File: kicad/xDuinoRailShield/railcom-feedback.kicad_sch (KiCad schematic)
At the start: 8 parts, among them Q2 S8050, Q3 S8550, Q4 S8050, Q5 S8550

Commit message: Shield extracted
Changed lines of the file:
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@@
     (stroke (width 0) (type default))
   )
-  (label "RailCom feedback channel" (at 100.33 44.45 0) (fields_autoplaced)
+  (label "RailCom feedback generator" (at 100.33 44.45 0) (fields_autoplaced)
     (effects (font (size 3 3)) (justify left bottom))
   )

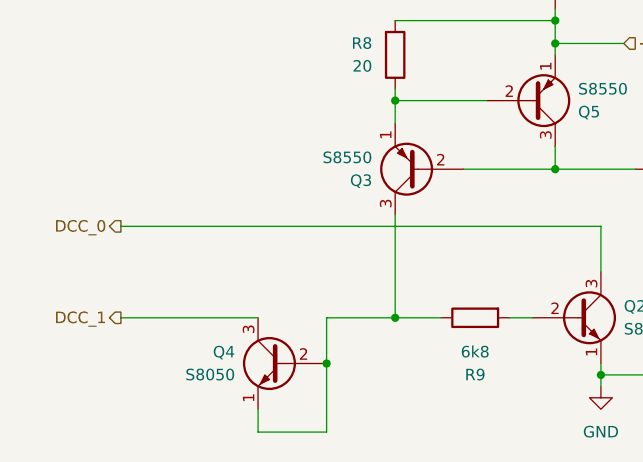
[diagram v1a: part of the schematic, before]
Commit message: More options, more Partnumbers
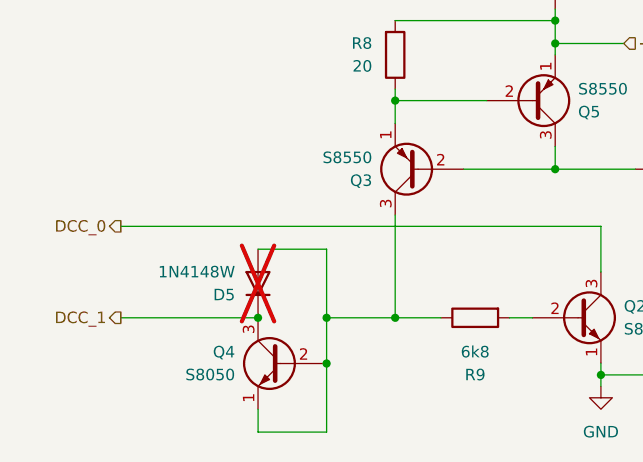
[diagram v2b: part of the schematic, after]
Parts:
- added D5: 1N4148W, Diode_SMD:D_SOD-123, symbol Diode:1N4148W
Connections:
- net DCC_1: now also D5.1 (K)
- net at Q3.3 (C), Q4.1 (E), Q4.2 (B)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: now also D5.2 (A)
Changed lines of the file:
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@@
   (junction (at 134.62 93.98) (diameter 0) (color 0 0 0 0)
   )
+  (junction (at 134.62 88.9) (diameter 0) (color 0 0 0 0)
+  )
+  (junction (at 127 88.9) (diameter 0) (color 0 0 0 0)
+  )
   (junction (at 160.02 72.39) (diameter 0) (color 0 0 0 0)
   )
@@
     (stroke (width 0) (type default))
   )
+  (wire (pts (xy 127 81.28) (xy 134.62 81.28))
+    (stroke (width 0) (type default))
+  )
   (wire (pts (xy 134.62 88.9) (xy 134.62 93.98))
     (stroke (width 0) (type default))
@@
   )
   (wire (pts (xy 181.61 72.39) (xy 176.53 72.39))
+    (stroke (width 0) (type default))
+  )
+  (wire (pts (xy 134.62 81.28) (xy 134.62 88.9))
     (stroke (width 0) (type default))
   )
@@
         )
         (path "/e63e39d7-6ac0-4ffd-8aa3-1841a4541b55/8dbd326e-72bb-40d4-858a-dc9fedaab895"
-          (reference "Q3") (unit 1)
+          (reference "Q403") (unit 1)
         )
       )
@@
         )
         (path "/e63e39d7-6ac0-4ffd-8aa3-1841a4541b55/8dbd326e-72bb-40d4-858a-dc9fedaab895"
-          (reference "Q2") (unit 1)
+          (reference "Q402") (unit 1)
         )
       )
@@
         )
         (path "/e63e39d7-6ac0-4ffd-8aa3-1841a4541b55/8dbd326e-72bb-40d4-858a-dc9fedaab895"
-          (reference "Q1") (unit 1)
+          (reference "Q401") (unit 1)
         )
       )
@@
         )
         (path "/e63e39d7-6ac0-4ffd-8aa3-1841a4541b55/8dbd326e-72bb-40d4-858a-dc9fedaab895"
-          (reference "R9") (unit 1)
+          (reference "R403") (unit 1)
         )
       )
@@
         )
         (path "/e63e39d7-6ac0-4ffd-8aa3-1841a4541b55/8dbd326e-72bb-40d4-858a-dc9fedaab895"
-          (reference "Q4") (unit 1)
+          (reference "Q404") (unit 1)
         )
       )
@@
         )
         (path "/e63e39d7-6ac0-4ffd-8aa3-1841a4541b55/8dbd326e-72bb-40d4-858a-dc9fedaab895"
-          (reference "#PWR012") (unit 1)
+          (reference "#PWR0402") (unit 1)
         )
       )
@@
         )
         (path "/e63e39d7-6ac0-4ffd-8aa3-1841a4541b55/8dbd326e-72bb-40d4-858a-dc9fedaab895"
-          (reference "#PWR011") (unit 1)
+          (reference "#PWR0401") (unit 1)
         )
       )
@@
         )
         (path "/e63e39d7-6ac0-4ffd-8aa3-1841a4541b55/8dbd326e-72bb-40d4-858a-dc9fedaab895"
-          (reference "R7") (unit 1)
+          (reference "R401") (unit 1)
         )
       )
@@
         )
         (path "/e63e39d7-6ac0-4ffd-8aa3-1841a4541b55/8dbd326e-72bb-40d4-858a-dc9fedaab895"
-          (reference "R8") (unit 1)
+          (reference "R402") (unit 1)
         )
       )
@@
         )
         (path "/e63e39d7-6ac0-4ffd-8aa3-1841a4541b55/8dbd326e-72bb-40d4-858a-dc9fedaab895"
-          (reference "JP_RAILCOM1") (unit 1)
-        )
-      )
+          (reference "JP_RAILCOM401") (unit 1)
+        )
+      )
+    )
+  )
+  (symbol (lib_id "Diode:1N4148W") (at 127 85.09 90) (unit 1)
+    (in_bom no) (on_board yes) (dnp yes)
+    (property "Reference" "D5" (at 124.46 86.36 90)
+      (effects (font (size 1.27 1.27)) (justify left))
+    )
+    (property "Value" "1N4148W" (at 124.46 83.82 90)
+      (effects (font (size 1.27 1.27)) (justify left))
+    )
+    (property "Footprint" "Diode_SMD:D_SOD-123" (at 131.445 85.09 0)
+      (effects (font (size 1.27 1.27)) hide)
+    )
+    (property "Datasheet" "https://www.vishay.com/docs/85748/1n4148w.pdf" (at 127 85.09 0)
+      (effects (font (size 1.27 1.27)) hide)
+    )
+    (property "Sim.Device" "D" (at 127 85.09 0)
+      (effects (font (size 1.27 1.27)) hide)
+    )
+    (property "Sim.Pins" "1=K 2=A" (at 127 85.09 0)
+      (effects (font (size 1.27 1.27)) hide)
+    )
+    (property "LCSC" "C81598" (at 127 85.09 0)
+      (effects (font (size 1.27 1.27)) hide)
+    )
+    (pin "2")
+    (pin "1")
+    (instances
+      (project "xDuinoRailShield"
+        (path "/e63e39d7-6ac0-4ffd-8aa3-1841a4541b55"
+          (reference "D5") (unit 1)
+        )
+        (path "/e63e39d7-6ac0-4ffd-8aa3-1841a4541b55/b84a333b-f29e-43df-b84d-edef752a64aa"
+          (reference "D301") (unit 1)
+        )
+        (path "/e63e39d7-6ac0-4ffd-8aa3-1841a4541b55/8dbd326e-72bb-40d4-858a-dc9fedaab895"
+          (reference "D401") (unit 1)
+        )
+      )

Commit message: Another iteration on the layout
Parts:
- renumbered D5 to D401, JP_RAILCOM1 to JP_RAILCOM401, Q4 to Q401, Q3 to Q402, Q5 to Q403, Q2 to Q404

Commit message: xXiaoCentralMini
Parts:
- removed JP_RAILCOM401: SolderJumper_2_Open, Jumper:SolderJumper-2_P1.3mm_Open_TrianglePad1.0x1.5mm, symbol Jumper:SolderJumper_2_Open
- R7, R8, R9: footprint Resistor_SMD:R_0805_2012Metric_Pad1.20x1.40mm_HandSolder -> Resistor_SMD:R_0603_1608Metric_Pad0.98x0.95mm_HandSolder
- renumbered D401 to D7, Q401 to Q2, Q402 to Q3, Q403 to Q4, Q404 to Q5
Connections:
- net RAILCOM_DATA: now also R7.2
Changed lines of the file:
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@@
-	(wire
-		(pts
-			(xy 181.61 72.39) (xy 176.53 72.39)
-		)
-		(stroke
-			(width 0)
-			(type default)
-		)
-	)
 	(wire
 		(pts
@@
 	(wire
 		(pts
-			(xy 190.5 72.39) (xy 189.23 72.39)
+			(xy 176.53 72.39) (xy 182.88 72.39)
 		)
 		(stroke
@@
 	(hierarchical_label "RAILCOM_DATA"
 		(shape input)
-		(at 190.5 72.39 0)
+		(at 182.88 72.39 0)
 		(fields_autoplaced yes)
 		(effects
@@
 		(on_board yes)
 		(dnp no)
-		(property "Reference" "Q403"
+		(property "Reference" "Q4"
 			(at 162.56 66.04 0)
 			(effects
@@
 			(project "xDuinoRailShield"
 				(path "/e63e39d7-6ac0-4ffd-8aa3-1841a4541b55/8dbd326e-72bb-40d4-858a-dc9fedaab895"
-					(reference "Q403")
+					(reference "Q4")
 					(unit 1)
 				)
@@
 		(on_board yes)
 		(dnp no)
-		(property "Reference" "Q402"
+		(property "Reference" "Q3"
 			(at 139.7 73.66 0)
 			(effects
@@
 			(project "xDuinoRailShield"
 				(path "/e63e39d7-6ac0-4ffd-8aa3-1841a4541b55/8dbd326e-72bb-40d4-858a-dc9fedaab895"
-					(reference "Q402")
+					(reference "Q3")
 					(unit 1)
 				)
@@
 		(on_board yes)
 		(dnp no)
-		(property "Reference" "Q401"
+		(property "Reference" "Q2"
 			(at 124.46 92.71 0)
 			(effects
@@
 			(project "xDuinoRailShield"
 				(path "/e63e39d7-6ac0-4ffd-8aa3-1841a4541b55/8dbd326e-72bb-40d4-858a-dc9fedaab895"
-					(reference "Q401")
+					(reference "Q2")
 					(unit 1)
 				)
@@
 			)
 		)
-		(property "Footprint" "Resistor_SMD:R_0805_2012Metric_Pad1.20x1.40mm_HandSolder"
+		(property "Footprint" "Resistor_SMD:R_0603_1608Metric_Pad0.98x0.95mm_HandSolder"
 			(at 172.72 74.168 90)
 			(effects
@@
 			(project "xDuinoRailShield"
 				(path "/e63e39d7-6ac0-4ffd-8aa3-1841a4541b55/8dbd326e-72bb-40d4-858a-dc9fedaab895"
-					(reference "R403")
+					(reference "R11")
 					(unit 1)
 				)
@@
 		(dnp no)
 		(fields_autoplaced yes)
-		(property "Reference" "Q404"
+		(property "Reference" "Q5"
 			(at 167.64 87.63 0)
 			(effects
@@
 			(project "xDuinoRailShield"
 				(path "/e63e39d7-6ac0-4ffd-8aa3-1841a4541b55/8dbd326e-72bb-40d4-858a-dc9fedaab895"
-					(reference "Q404")
+					(reference "Q5")
 					(unit 1)
 				)
@@
 			(project "xDuinoRailShield"
 				(path "/e63e39d7-6ac0-4ffd-8aa3-1841a4541b55/8dbd326e-72bb-40d4-858a-dc9fedaab895"
-					(reference "#PWR0402")
+					(reference "#PWR024")
 					(unit 1)
 				)
@@
 			(project "xDuinoRailShield"
 				(path "/e63e39d7-6ac0-4ffd-8aa3-1841a4541b55/8dbd326e-72bb-40d4-858a-dc9fedaab895"
-					(reference "#PWR0401")
+					(reference "#PWR023")
 					(unit 1)
 				)
@@
 			)
 		)
-		(property "Footprint" "Resistor_SMD:R_0805_2012Metric_Pad1.20x1.40mm_HandSolder"
+		(property "Footprint" "Resistor_SMD:R_0603_1608Metric_Pad0.98x0.95mm_HandSolder"
 			(at 140.462 59.69 90)
 			(effects
@@
 			(project "xDuinoRailShield"
 				(path "/e63e39d7-6ac0-4ffd-8aa3-1841a4541b55/8dbd326e-72bb-40d4-858a-dc9fedaab895"
-					(reference "R401")
+					(reference "R9")
 					(unit 1)
 				)
@@
 			)
 		)
-		(property "Footprint" "Resistor_SMD:R_0805_2012Metric_Pad1.20x1.40mm_HandSolder"
+		(property "Footprint" "Resistor_SMD:R_0603_1608Metric_Pad0.98x0.95mm_HandSolder"
 			(at 151.13 87.122 90)
 			(effects
@@
 			(project "xDuinoRailShield"
 				(path "/e63e39d7-6ac0-4ffd-8aa3-1841a4541b55/8dbd326e-72bb-40d4-858a-dc9fedaab895"
-					(reference "R402")
-					(unit 1)
-				)
-			)
-		)
-	)
-	(symbol
-		(lib_id "Jumper:SolderJumper_2_Open")
-		(at 185.42 72.39 0)
-		(mirror x)
-		(unit 1)
-		(exclude_from_sim no)
-		(in_bom yes)
-		(on_board yes)
-		(dnp no)
-		(property "Reference" "JP_RAILCOM401"
-			(at 185.42 78.74 0)
-			(effects
-				(font
-					(size 1.27 1.27)
-				)
-			)
-		)
-		(property "Value" "SolderJumper_2_Open"
-			(at 185.42 76.2 0)
-			(effects
-				(font
-					(size 1.27 1.27)
-				)
-			)
-		)
-		(property "Footprint" "Jumper:SolderJumper-2_P1.3mm_Open_TrianglePad1.0x1.5mm"
-			(at 185.42 72.39 0)
-			(effects
-				(font
-					(size 1.27 1.27)
-				)
-				(hide yes)
-			)
-		)
-		(property "Datasheet" "~"
-			(at 185.42 72.39 0)
-			(effects
-				(font
-					(size 1.27 1.27)
-				)
-				(hide yes)
-			)
-		)
-		(property "Description" ""
-			(at 185.42 72.39 0)
-			(effects
-				(font
-					(size 1.27 1.27)
-				)
-				(hide yes)
-			)
-		)
-		(property "LCSC" ""
-			(at 185.42 72.39 0)
-			(effects
-				(font
-					(size 1.27 1.27)
-				)
-				(hide yes)
-			)
-		)
-		(pin "1"
-		)
-		(pin "2"
-		)
-		(instances
-			(project "xDuinoRailShield"
-				(path "/e63e39d7-6ac0-4ffd-8aa3-1841a4541b55/8dbd326e-72bb-40d4-858a-dc9fedaab895"
-					(reference "JP_RAILCOM401")
+					(reference "R10")
 					(unit 1)
 				)
@@
 		(exclude_from_sim no)
 		(in_bom no)
-		(on_board yes)
+		(on_board no)
 		(dnp yes)
-		(property "Reference" "D401"
+		(property "Reference" "D7"
 			(at 124.46 86.36 90)
 			(effects
@@
 			(project "xDuinoRailShield"
 				(path "/e63e39d7-6ac0-4ffd-8aa3-1841a4541b55/8dbd326e-72bb-40d4-858a-dc9fedaab895"
-					(reference "D401")
-					(unit 1)
-				)
+					(reference "D7")
+					(unit 1)
+				)

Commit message: More nice changes
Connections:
- net DCC_0 renamed DCC0
- net DCC_1 renamed DCC1
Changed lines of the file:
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@@
 		(color 0 0 0 0)
 	)
+	(bus_entry
+		(at 109.22 86.36)
+		(size 2.54 2.54)
+		(stroke
+			(width 0)
+			(type default)
+		)
+	)
+	(bus_entry
+		(at 109.22 76.2)
+		(size 2.54 2.54)
+		(stroke
+			(width 0)
+			(type default)
+		)
+	)
+	(bus
+		(pts
+			(xy 109.22 72.39) (xy 109.22 76.2)
+		)
+		(stroke
+			(width 0)
+			(type default)
+		)
+	)
 	(wire
 		(pts
@@
 		)
 	)
+	(bus
+		(pts
+			(xy 109.22 76.2) (xy 109.22 86.36)
+		)
+		(stroke
+			(width 0)
+			(type default)
+		)
+	)
 	(wire
 		(pts
@@
 		)
 	)
+	(bus
+		(pts
+			(xy 105.41 69.85) (xy 106.68 69.85)
+		)
+		(stroke
+			(width 0)
+			(type default)
+		)
+	)
 	(wire
 		(pts
@@
 		)
 	)
+	(bus
+		(pts
+			(xy 106.68 69.85) (xy 109.22 72.39)
+		)
+		(stroke
+			(width 0)
+			(type default)
+		)
+	)
 	(wire
 		(pts
@@
 		)
 	)
+	(label "DCC0"
+		(at 114.3 78.74 0)
+		(fields_autoplaced yes)
+		(effects
+			(font
+				(size 1.27 1.27)
+			)
+			(justify left bottom)
+		)
+	)
+	(label "DCC1"
+		(at 114.3 88.9 0)
+		(fields_autoplaced yes)
+		(effects
+			(font
+				(size 1.27 1.27)
+			)
+			(justify left bottom)
+		)
+	)
 	(label "RailCom feedback generator"
-		(at 100.33 44.45 0)
+		(at 110.49 45.72 0)
 		(fields_autoplaced yes)
 		(effects
@@
 		)
 	)
-	(hierarchical_label "DCC_1"
+	(hierarchical_label "DCC[0..1]"
 		(shape output)
-		(at 111.76 88.9 180)
+		(at 105.41 69.85 180)
 		(fields_autoplaced yes)
 		(effects
-			(font
-				(size 1.27 1.27)
-			)
-			(justify right)
-		)
-	)
-	(hierarchical_label "DCC_0"
-		(shape output)
-		(at 111.76 78.74 180)
-		(fields_autoplaced yes)
-		(effects

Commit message: More busses added
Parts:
- renumbered D7 to D501, Q2 to Q501, Q3 to Q502, Q4 to Q503, Q5 to Q504
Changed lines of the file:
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@@
 		(on_board yes)
 		(dnp no)
-		(property "Reference" "Q4"
+		(property "Reference" "Q503"
 			(at 162.56 66.04 0)
 			(effects
@@
 			(project "xDuinoRailShield"
 				(path "/e63e39d7-6ac0-4ffd-8aa3-1841a4541b55/8dbd326e-72bb-40d4-858a-dc9fedaab895"
-					(reference "Q4")
+					(reference "Q503")
 					(unit 1)
 				)
@@
 		(on_board yes)
 		(dnp no)
-		(property "Reference" "Q3"
+		(property "Reference" "Q502"
 			(at 139.7 73.66 0)
 			(effects
@@
 			(project "xDuinoRailShield"
 				(path "/e63e39d7-6ac0-4ffd-8aa3-1841a4541b55/8dbd326e-72bb-40d4-858a-dc9fedaab895"
-					(reference "Q3")
+					(reference "Q502")
 					(unit 1)
 				)
@@
 		(on_board yes)
 		(dnp no)
-		(property "Reference" "Q2"
+		(property "Reference" "Q501"
 			(at 124.46 92.71 0)
 			(effects
@@
 			(project "xDuinoRailShield"
 				(path "/e63e39d7-6ac0-4ffd-8aa3-1841a4541b55/8dbd326e-72bb-40d4-858a-dc9fedaab895"
-					(reference "Q2")
+					(reference "Q501")
 					(unit 1)
 				)
@@
 			(project "xDuinoRailShield"
 				(path "/e63e39d7-6ac0-4ffd-8aa3-1841a4541b55/8dbd326e-72bb-40d4-858a-dc9fedaab895"
-					(reference "R11")
+					(reference "R503")
 					(unit 1)
 				)
@@
 		(dnp no)
 		(fields_autoplaced yes)
-		(property "Reference" "Q5"
+		(property "Reference" "Q504"
 			(at 167.64 87.63 0)
 			(effects
@@
 			(project "xDuinoRailShield"
 				(path "/e63e39d7-6ac0-4ffd-8aa3-1841a4541b55/8dbd326e-72bb-40d4-858a-dc9fedaab895"
-					(reference "Q5")
+					(reference "Q504")
 					(unit 1)
 				)
@@
 			(project "xDuinoRailShield"
 				(path "/e63e39d7-6ac0-4ffd-8aa3-1841a4541b55/8dbd326e-72bb-40d4-858a-dc9fedaab895"
-					(reference "#PWR024")
+					(reference "#PWR0502")
 					(unit 1)
 				)
@@
 			(project "xDuinoRailShield"
 				(path "/e63e39d7-6ac0-4ffd-8aa3-1841a4541b55/8dbd326e-72bb-40d4-858a-dc9fedaab895"
-					(reference "#PWR023")
+					(reference "#PWR0501")
 					(unit 1)
 				)
@@
 			(project "xDuinoRailShield"
 				(path "/e63e39d7-6ac0-4ffd-8aa3-1841a4541b55/8dbd326e-72bb-40d4-858a-dc9fedaab895"
-					(reference "R9")
+					(reference "R501")
 					(unit 1)
 				)
@@
 			(project "xDuinoRailShield"
 				(path "/e63e39d7-6ac0-4ffd-8aa3-1841a4541b55/8dbd326e-72bb-40d4-858a-dc9fedaab895"
-					(reference "R10")
+					(reference "R502")
 					(unit 1)
 				)
@@
 		(on_board no)
 		(dnp yes)
-		(property "Reference" "D7"
+		(property "Reference" "D501"
 			(at 124.46 86.36 90)
 			(effects
@@
 			(project "xDuinoRailShield"
 				(path "/e63e39d7-6ac0-4ffd-8aa3-1841a4541b55/8dbd326e-72bb-40d4-858a-dc9fedaab895"
-					(reference "D7")
-					(unit 1)
-				)
+					(reference "D501")
+					(unit 1)
+				)

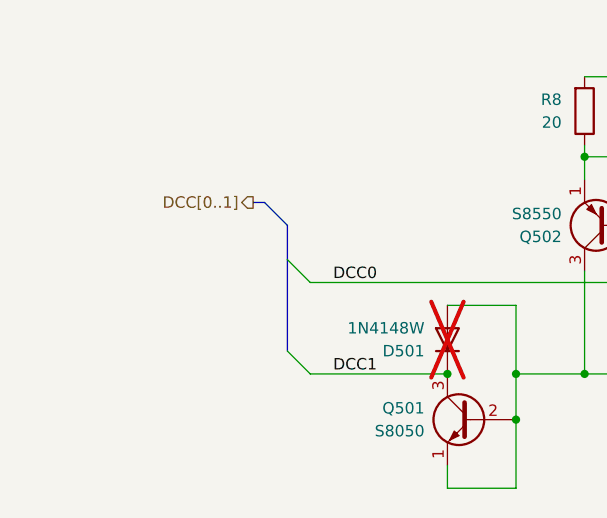
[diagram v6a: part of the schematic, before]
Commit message: Draft of loco decoder
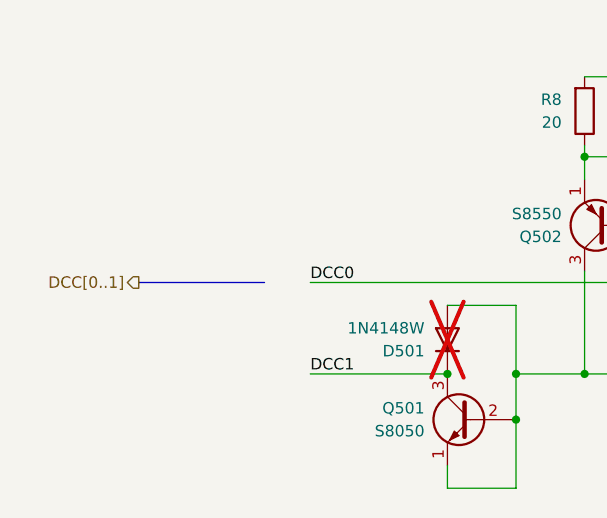
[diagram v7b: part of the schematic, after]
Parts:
- R7, R8, R9: footprint Resistor_SMD:R_0603_1608Metric_Pad0.98x0.95mm_HandSolder -> Resistor_SMD:R_0805_2012Metric_Pad1.20x1.40mm_HandSolder

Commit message: A lot of fixes
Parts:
- renumbered D501 to D401, Q501 to Q401, Q502 to Q402, Q503 to Q403, Q504 to Q404
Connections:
- net RC_CURR: now reaches Q402.1 (E), Q403.2 (B), R8.1
- net RC_FB_IN: now reaches Q402.2 (B), Q403.3 (C), R7.1
- net RC_SIGNAL: now reaches D401.2 (A), Q401.1 (E), Q401.2 (B), Q402.3 (C), R9.1
- net RC_ON_OFF: now reaches Q404.2 (B), R9.2
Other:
- note added: "RailCom feedback generator"
- moved on the sheet: D401, Q401, Q402, Q403, Q404, R7, R8, R9
